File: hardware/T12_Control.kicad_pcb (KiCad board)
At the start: 2 copper layers, 49.5 x 38.2 mm, 49 parts, among them J1 Screw_Terminal_01x02, J2 GX12-5M, J3 SPI LCD, J4 I2C LCD, J5 SWD, J6 Serial, Q1 TPC8107, Q2 BC817, U1 SPX2954M3-3.3_SOT223, U2 24LC32, U3 SGM8551XN, U4 STM32F103CBTx

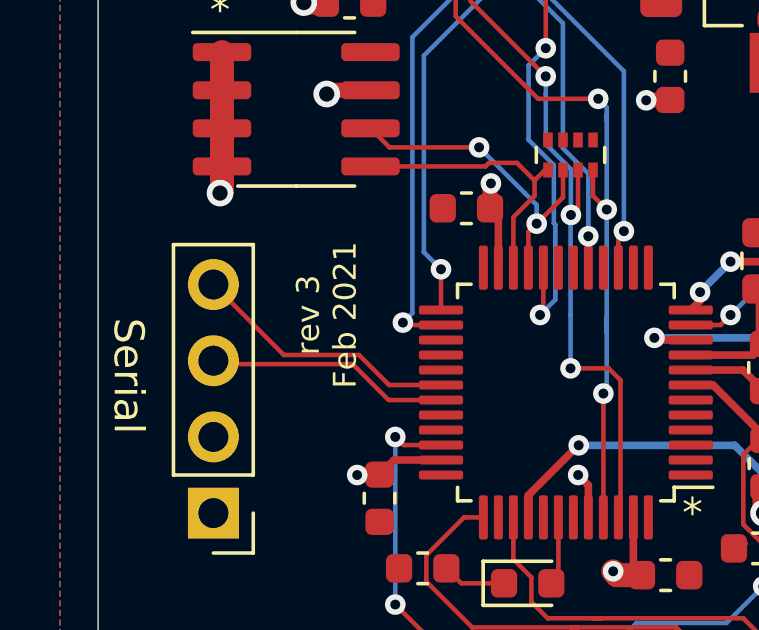
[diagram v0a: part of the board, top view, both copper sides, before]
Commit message: Start soldering Iron rev 4.
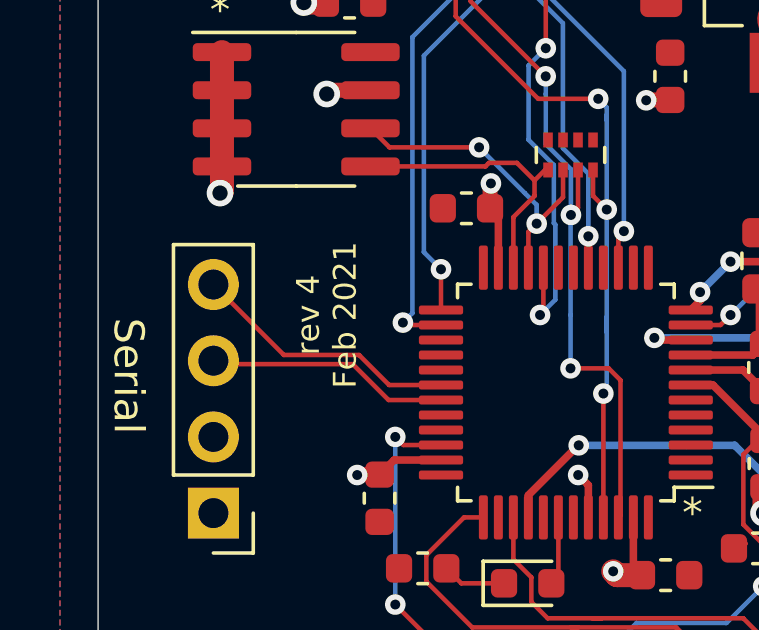
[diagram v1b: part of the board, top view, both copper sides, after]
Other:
- board text added: "rev 4 Feb 2021"
- board text removed: "rev 3 Feb 2021"
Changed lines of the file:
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@@
     (effects (font (size 1 1) (thickness 0.15)) (justify mirror))
   )
-  (gr_text "rev 3\nFeb 2021" (at 203.2 92.456 90) (layer "F.SilkS")
+  (gr_text "rev 4\nFeb 2021" (at 203.2 92.456 90) (layer "F.SilkS")
     (effects (font (size 0.762 0.762) (thickness 0.1016)))
   )

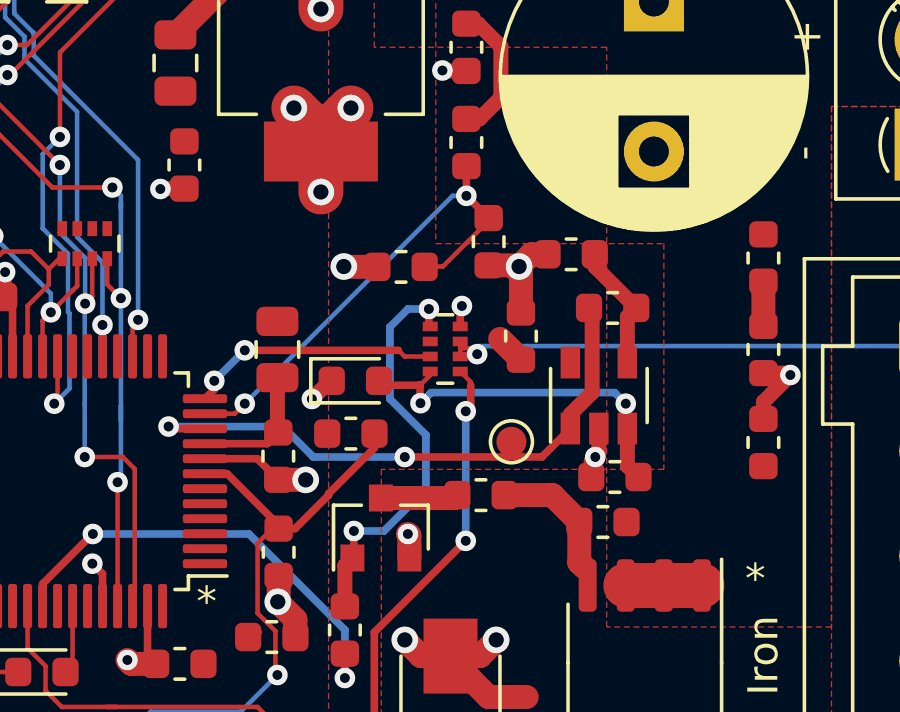
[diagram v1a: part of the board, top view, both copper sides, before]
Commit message: Added more ferrite beads to critical power lines.
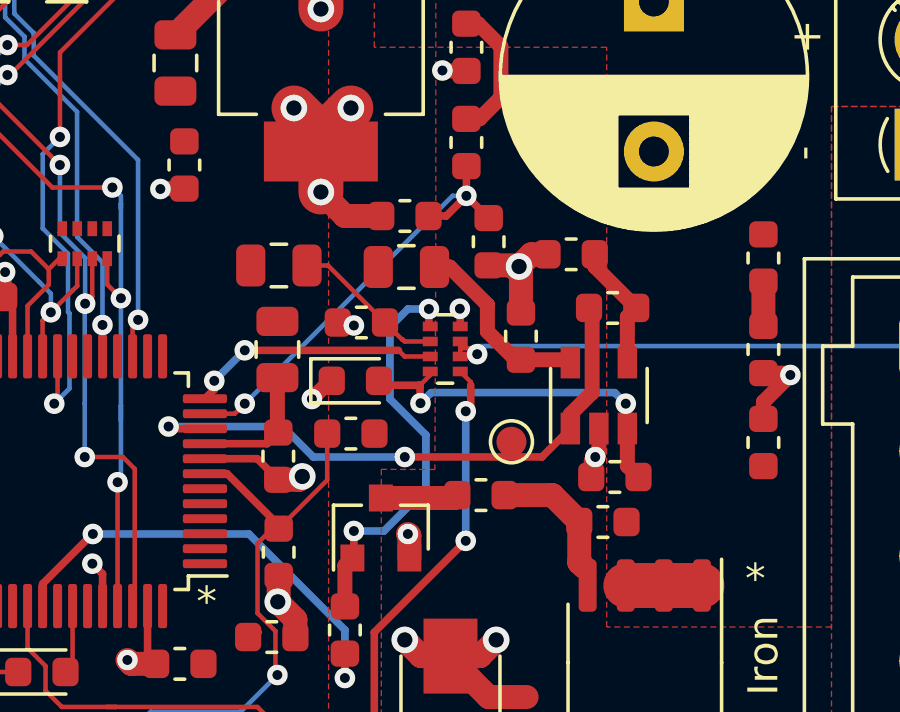
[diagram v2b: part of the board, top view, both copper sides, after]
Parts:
- added C18: 10nF, Capacitor_SMD:C_0603_1608Metric, F.Cu at (220.6, 89.8)
- added FB3: Ferrite_Bead, Inductor_SMD:L_0805_2012Metric, F.Cu at (222.1, 87.9)
- added FB4: Ferrite_Bead, Inductor_SMD:L_0805_2012Metric, F.Cu at (217.8, 87.8)
- C10: value 100nF -> 10nF
- moved C4 1.70 mm to (222.0, 86.2)
- turned R7 to 180 degrees
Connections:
- C13 pad 1: /3.3V -> Net-(C13-Pad1)
- RN1 pad 2: /3.3V -> Net-(C18-Pad1)
- U3 pad 5: /3.3V -> Net-(C13-Pad1)
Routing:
- net Net-(C13-Pad1): track 0.00 -> 6.37 mm
- net Net-(C18-Pad1): track 0.00 -> 5.16 mm
- net GND: track 52.0 -> 53.7 mm
- net /V_MON: track 16.6 -> 15.4 mm
- net /3.3V: track 1.10 -> 0.11 mm
- net /~NRST: track 21.2 -> 20.3 mm

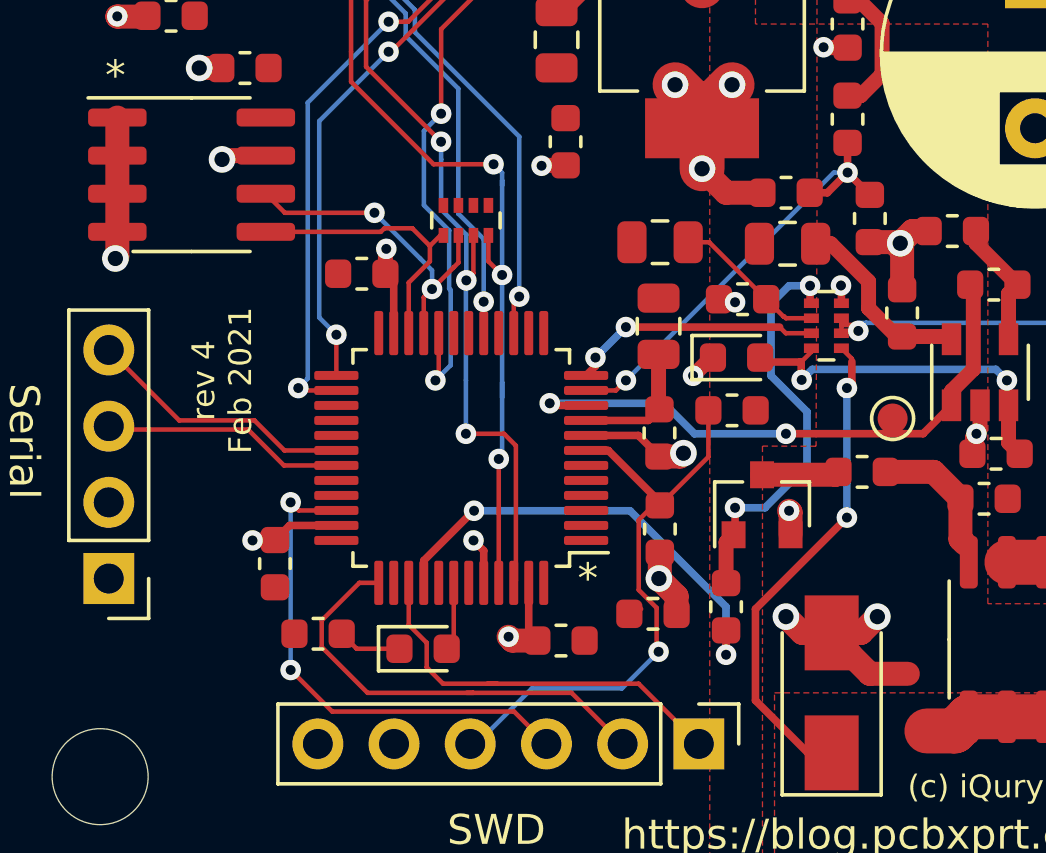
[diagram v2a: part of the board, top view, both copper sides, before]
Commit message: Update layout for power traces.
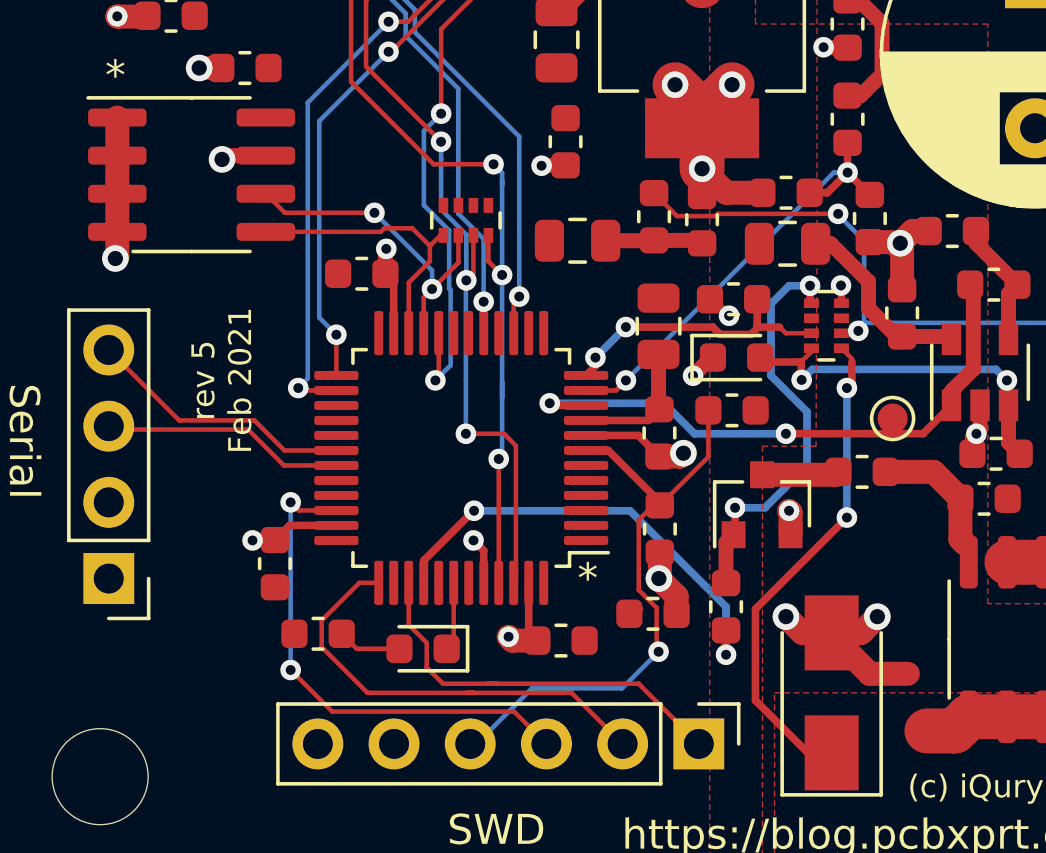
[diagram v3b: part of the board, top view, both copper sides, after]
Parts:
- added C19: 1uF, Capacitor_SMD:C_0603_1608Metric, F.Cu at (220.2, 89.8)
- added R11: 4.7k 1%, Resistor_SMD:R_0603_1608Metric, F.Cu at (217.6, 87.0)
- moved C18 2.97 mm to (219.2, 87.1), turned to 90 degrees
- moved FB4 2.75 mm to (215.1, 87.8)
- turned D3 to 180 degrees
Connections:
- R9 pad 1: Net-(D3-Pad1) -> Net-(D3-Pad2)
- RN1 pad 2: Net-(C18-Pad1) -> (no net)
- RN1 pad 7: Net-(J2-Pad1) -> (no net)
- U4 pad 42: Net-(D3-Pad2) -> Net-(D3-Pad1)
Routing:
- net Net-(J2-Pad1): track 16.9 -> 27.4 mm, vias 1 -> 2
- net Net-(C18-Pad1): track 5.16 -> 3.26 mm
- net /NTC: track 8.43 -> 9.58 mm
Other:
- board text added: "rev 5 Feb 2021"
- board text removed: "rev 4 Feb 2021"

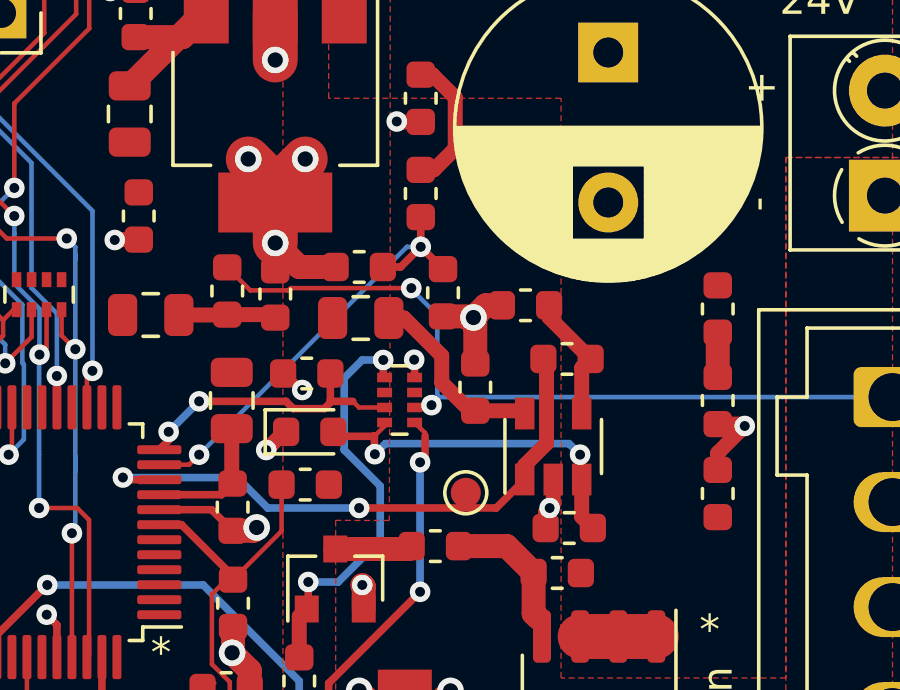
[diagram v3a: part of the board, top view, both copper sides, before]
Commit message: Switch iron to 4 layer. Add dedicated GNDA signal.
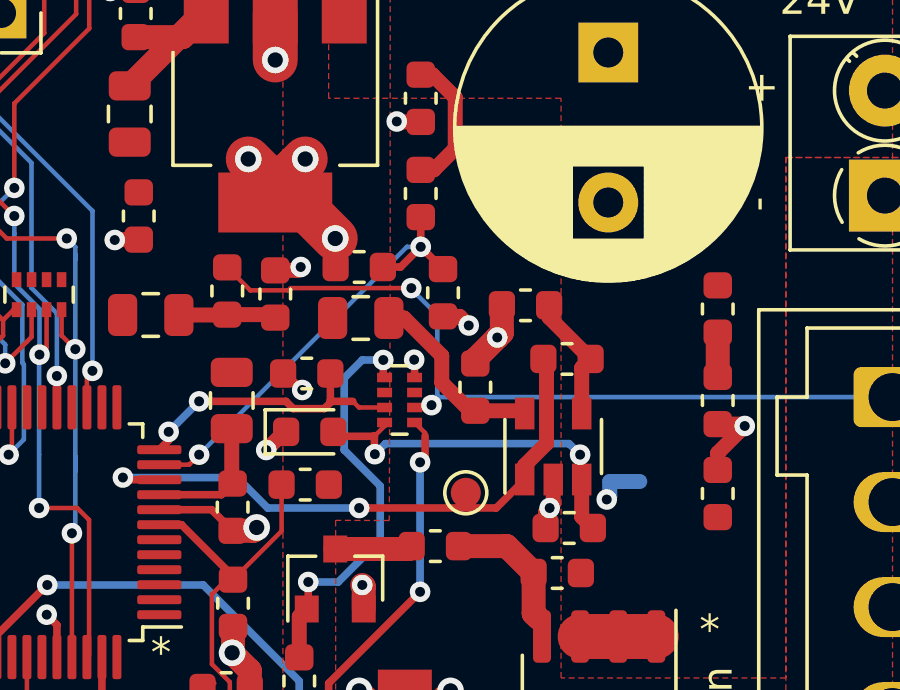
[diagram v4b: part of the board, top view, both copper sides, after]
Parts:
- added NT1: Net-Tie_2, NetTie:NetTie-2_SMD_Pad0.5mm, B.Cu at (230.8, 93.3)
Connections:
- net /D/~C renamed /D/~{C}
- net /~CS renamed /~{CS}
- net /~NRST renamed /~{NRST}
- net /~RST renamed /~{RST}
- C10 pad 2: GND -> GNDA
- C13 pad 2: GND -> GNDA
- C15 pad 2: GND -> GNDA
- C18 pad 2: GND -> GNDA
- D2 pad 1: GND -> GNDA
- R5 pad 2: GND -> GNDA
- U3 pad 2: GND -> GNDA
- U4 pad 8: GND -> GNDA
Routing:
- net GNDA: track 0.00 -> 10.1 mm, vias 0 -> 6
- net GND: track 54.0 -> 44.6 mm, vias 26 -> 23
- added copper zone on In1.Cu, net GND
- added copper zone on In2.Cu, net GND
- added copper zone on In1.Cu, net GNDA
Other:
- copper layers 2 -> 4
- board text added: "D/~{C}"
- board text added: "~{CS}"
- board text added: "~{RESET}"
- board text added: "~{RST}"
- board text removed: "D/~C"
- board text removed: "~CS"
- board text removed: "~RESET"
- board text removed: "~RST"

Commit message: Update Iron gerbers, start new Iron revision.
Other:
- board text added: "rev 6 Jul 2021"
- board text removed: "rev 5 Feb 2021"
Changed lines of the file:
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@@
     (effects (font (size 1 1) (thickness 0.15)) (justify mirror))
   )
-  (gr_text "rev 5\nFeb 2021" (at 203.2 92.456 90) (layer "F.SilkS")
+  (gr_text "rev 6\nJul 2021" (at 203.2 92.456 90) (layer "F.SilkS")
     (effects (font (size 0.762 0.762) (thickness 0.1016)))
   )
@@
   (segment (start 219.716558 86.90362) (end 219.641558 86.97862) (width 0.1524) (layer "F.Cu") (net 23))
   (segment (start 219.641558 86.97862) (end 218.36612 86.97862) (width 0.1524) (layer "F.Cu") (net 23))
-  (segment (start 224.331259 90.882741) (end 224.409 90.805) (width 0.254) (layer "F.Cu") (net 23))
-  (segment (start 223.844503 90.882741) (end 224.331259 90.882741) (width 0.254) (layer "F.Cu") (net 23))
-  (segment (start 224.409 90.805) (end 224.211497 90.607497) (width 0.1524) (layer "F.Cu") (net 23))
   (segment (start 218.36612 86.97862) (end 217.6 86.2125) (width 0.1524) (layer "F.Cu") (net 23))
+  (segment (start 223.844503 90.882741) (end 224.532741 90.882741) (width 0.254) (layer "F.Cu") (net 23))
+  (segment (start 224.532741 90.882741) (end 224.55 90.9) (width 0.254) (layer "F.Cu") (net 23))
   (segment (start 223.735139 86.90362) (end 219.716558 86.90362) (width 0.1524) (layer "F.Cu") (net 23))
   (segment (start 223.735248 86.903511) (end 223.735139 86.90362) (width 0.1524) (layer "F.Cu") (net 23))
+  (via (at 224.55 90.9) (size 0.6858) (drill 0.3302) (layers "F.Cu" "B.Cu") (net 23))
   (via (at 223.735248 86.903511) (size 0.6858) (drill 0.3302) (layers "F.Cu" "B.Cu") (net 23))
-  (via (at 224.409 90.805) (size 0.6858) (drill 0.3302) (layers "F.Cu" "B.Cu") (net 23))
-  (segment (start 224.678 90.536) (end 224.424 90.536) (width 0.1524) (layer "B.Cu") (net 23))
-  (segment (start 239.776 90.536) (end 224.902 90.536) (width 0.1524) (layer "B.Cu") (net 23))
-  (segment (start 224.6 87.8) (end 223.735248 86.935248) (width 0.1524) (layer "B.Cu") (net 23))
-  (segment (start 224.409 90.805) (end 224.6 90.614) (width 0.1524) (layer "B.Cu") (net 23))
-  (segment (start 224.902 90.536) (end 224.678 90.536) (width 0.1524) (layer "B.Cu") (net 23))
-  (segment (start 223.735248 86.935248) (end 223.735248 86.903511) (width 0.1524) (layer "B.Cu") (net 23))
-  (segment (start 224.678 90.536) (end 224.409 90.805) (width 0.1524) (layer "B.Cu") (net 23))
-  (segment (start 224.6 90.614) (end 224.6 87.8) (width 0.1524) (layer "B.Cu") (net 23))
+  (segment (start 225.786 90.536) (end 224.914 90.536) (width 0.1524) (layer "B.Cu") (net 23))
+  (segment (start 239.776 90.536) (end 225.786 90.536) (width 0.1524) (layer "B.Cu") (net 23))
+  (segment (start 224.914 90.536) (end 224.55 90.9) (width 0.1524) (layer "B.Cu") (net 23))
+  (segment (start 223.735248 86.903511) (end 223.735248 86.935248) (width 0.1524) (layer "B.Cu") (net 23))
+  (segment (start 223.735248 86.935248) (end 224.6 87.8) (width 0.1524) (layer "B.Cu") (net 23))
+  (segment (start 224.6 87.8) (end 224.6 90.85) (width 0.1524) (layer "B.Cu") (net 23))
+  (segment (start 224.6 90.85) (end 224.55 90.9) (width 0.1524) (layer "B.Cu") (net 23))
   (segment (start 221.991581 90.882741) (end 221.78684 90.678) (width 0.1524) (layer "F.Cu") (net 24))
   (segment (start 215.646 91.694) (end 215.646 91.979) (width 0.254) (layer "F.Cu") (net 24))
@@
   (segment (start 217.407909 93.79) (end 217.779899 93.41801) (width 0.254) (layer "F.Cu") (net 34))
   (segment (start 215.335 93.79) (end 217.407909 93.79) (width 0.254) (layer "F.Cu") (net 34))
+  (segment (start 227.423345 90.992488) (end 227.515247 91.08439) (width 0.5) (layer "F.Cu") (net 35))
+  (segment (start 224.75 89.156024) (end 224.75 90.05) (width 0.5) (layer "F.Cu") (net 35))
+  (segment (start 225.868516 90.992488) (end 227.423345 90.992488) (width 0.5) (layer "F.Cu") (net 35))
+  (segment (start 225.031227 90.155199) (end 225.868516 90.992488) (width 0.5) (layer "F.Cu") (net 35))
+  (segment (start 224.855199 90.155199) (end 225.031227 90.155199) (width 0.5) (layer "F.Cu") (net 35))
+  (segment (start 222.9875 87.9) (end 223.493976 87.9) (width 0.5) (layer "F.Cu") (net 35))
+  (segment (start 224.75 90.05) (end 224.855199 90.155199) (width 0.5) (layer "F.Cu") (net 35))
   (segment (start 223.493976 87.9) (end 224.75 89.156024) (width 0.5) (layer "F.Cu") (net 35))
-  (segment (start 224.75 89.156024) (end 224.75 90.05) (width 0.5) (layer "F.Cu") (net 35))
-  (segment (start 227.423345 90.992488) (end 227.515247 91.08439) (width 0.5) (layer "F.Cu") (net 35))
-  (segment (start 225.868516 90.992488) (end 227.423345 90.992488) (width 0.5) (layer "F.Cu") (net 35))
-  (segment (start 222.9875 87.9) (end 223.493976 87.9) (width 0.5) (layer "F.Cu") (net 35))
-  (segment (start 225.692488 90.992488) (end 225.868516 90.992488) (width 0.5) (layer "F.Cu") (net 35))
-  (segment (start 224.75 90.05) (end 225.692488 90.992488) (width 0.5) (layer "F.Cu") (net 35))
   (segment (start 217.6 87.7875) (end 219.1 87.7875) (width 0.5) (layer "F.Cu") (net 36))
   (segment (start 215.9875 87.8) (end 217.5875 87.8) (width 0.5) (layer "F.Cu") (net 36))
